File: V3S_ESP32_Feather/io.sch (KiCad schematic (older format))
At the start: 21 parts, among them J3 CAM, J7 Micro_SD_Card_Det, J9 I2C, U1 V3S, Y1 X1E0000210832, Y2 CC5V-T1A 32.768KHZ +-20PPM 12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

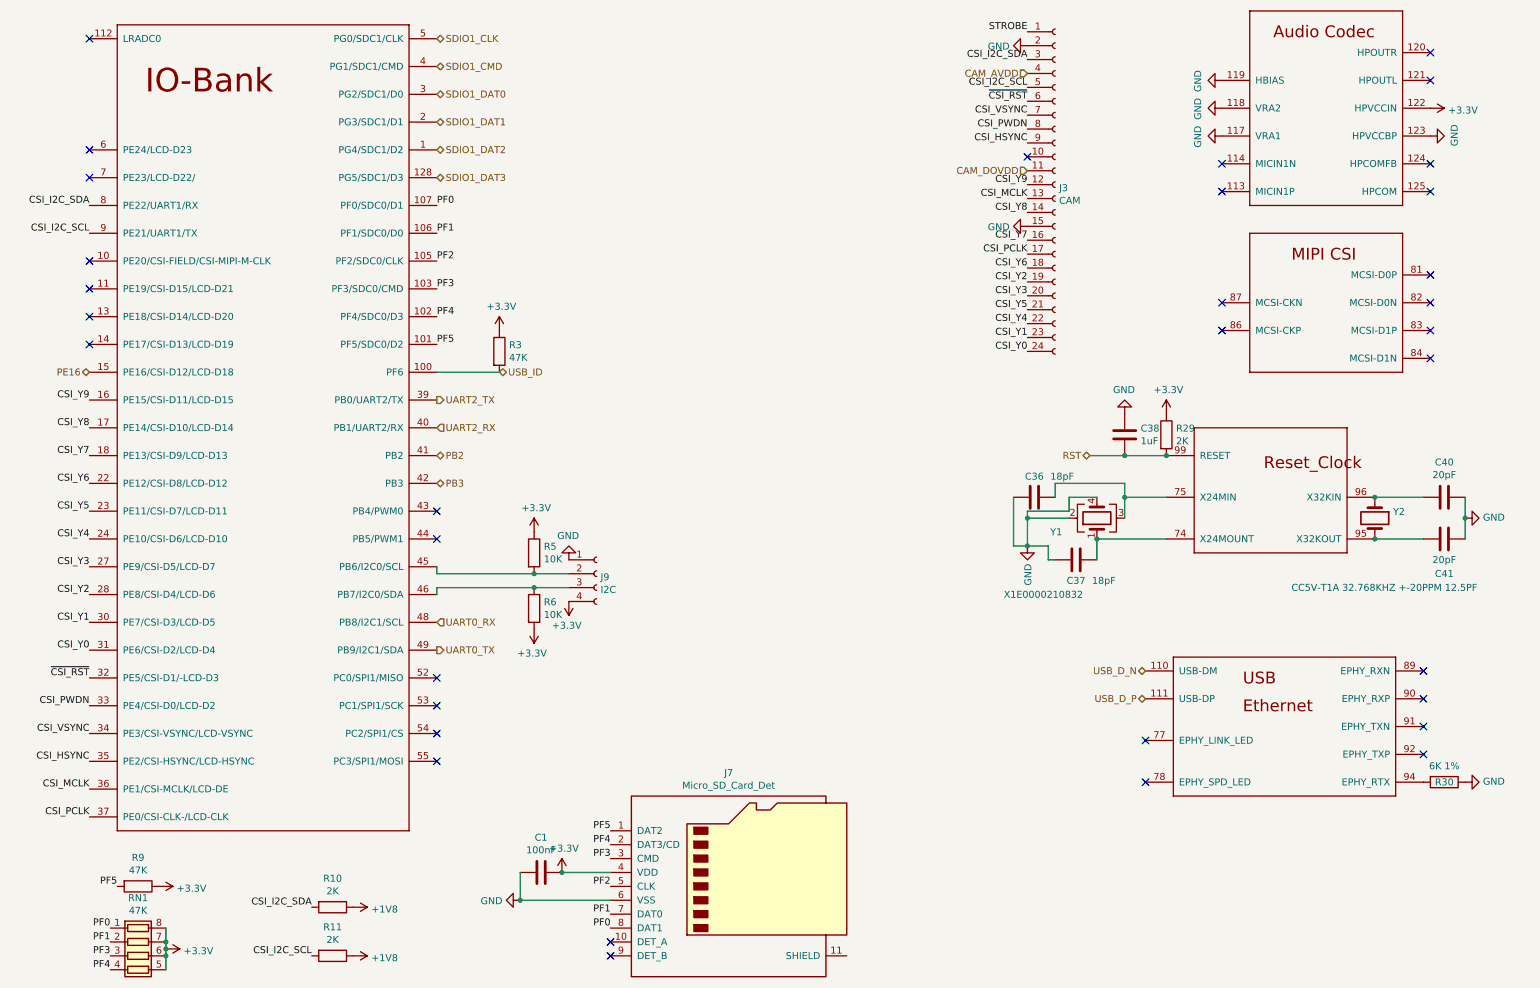
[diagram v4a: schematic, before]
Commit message: routing done, started filling bom
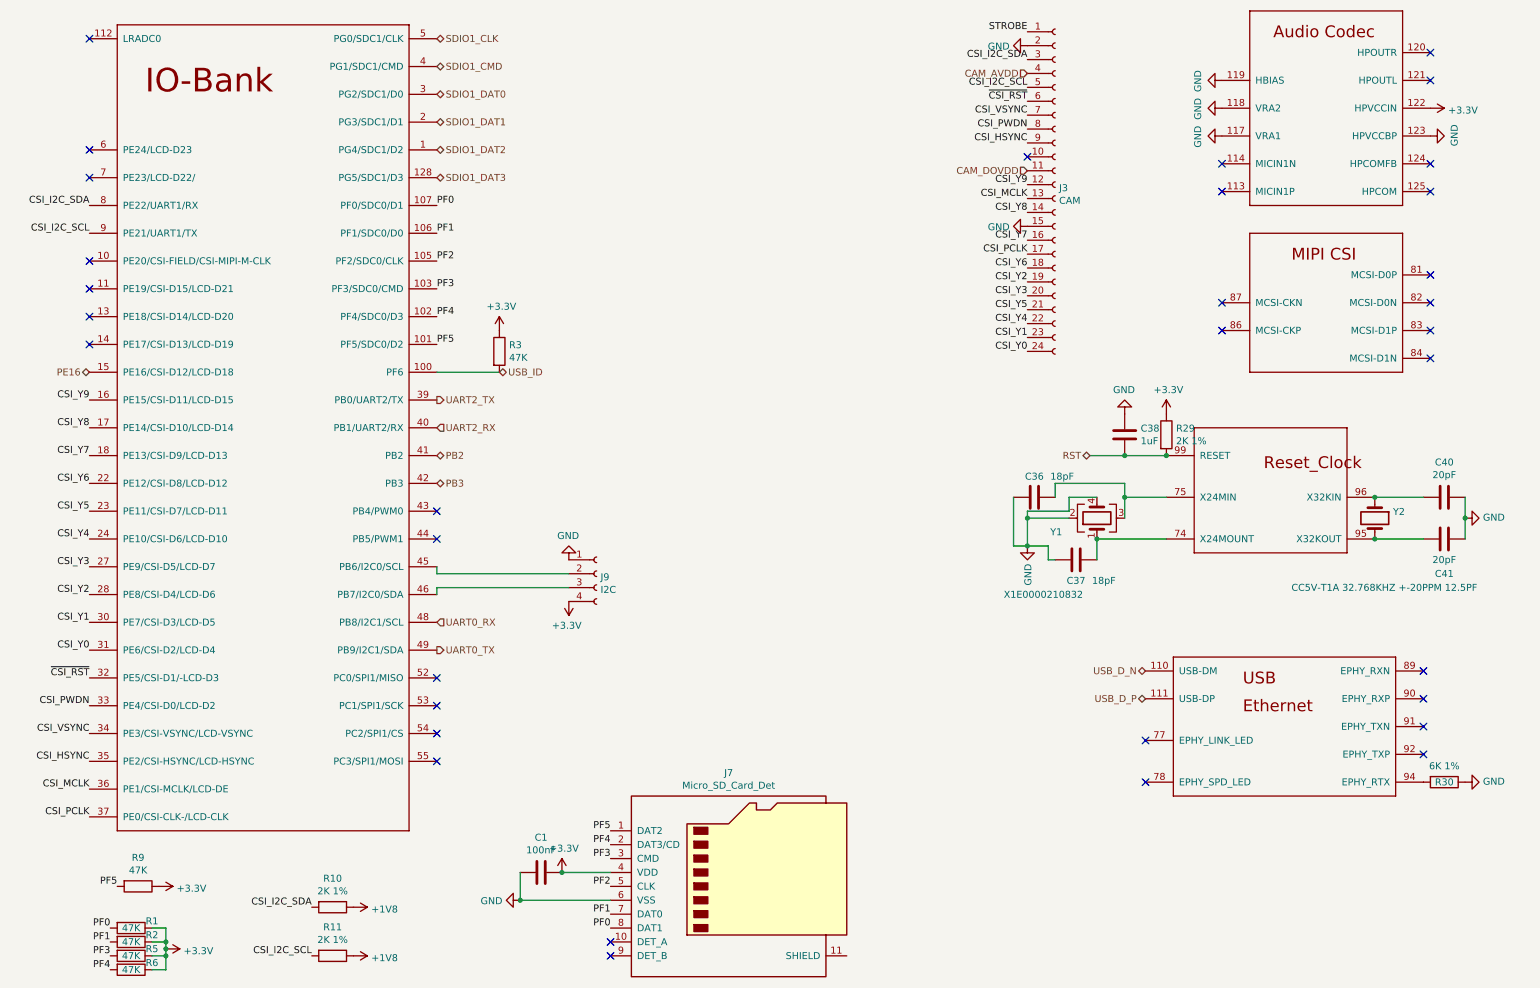
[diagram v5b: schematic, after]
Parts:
- removed RN1: 47K, Resistor_SMD:R_Array_Concave_4x0402, symbol Device:R_Pack04
- added R1, R2: 47K, Resistor_SMD:R_0201_0603Metric, symbol Device:R
- R10, R11, R29: value 2K -> 2K 1%
- R5, R6: value 10K -> 47K
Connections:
- net +3V3: now also R6.1, R1.1, R2.1; no longer R6.2
- net PF0: now also R1.2
- net PF1: now also R2.2
- net PF3: now also R5.2
- net PF4: now also R6.2
- net at J9.2 (Pin_2), U1.45 (PB6/I2C0/SCL): no longer R5.2
- net at J9.3 (Pin_3), U1.46 (PB7/I2C0/SDA): no longer R6.1
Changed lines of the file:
@@
 P 8750 3600
 F 0 "R29" H 8820 3646 50  0000 L CNN
-F 1 "2K" H 8820 3555 50  0000 L CNN
+F 1 "2K 1%" H 8820 3555 50  0000 L CNN
 F 2 "Resistor_SMD:R_0201_0603Metric" V 8680 3600 50  0001 C CNN
 F 3 "~" H 8750 3600 50  0001 C CNN
@@
 P 2750 7000
 F 0 "R10" V 2543 7000 50  0000 C CNN
-F 1 "2K" V 2634 7000 50  0000 C CNN
+F 1 "2K 1%" V 2634 7000 50  0000 C CNN
 F 2 "Resistor_SMD:R_0201_0603Metric" V 2680 7000 50  0001 C CNN
 F 3 "~" H 2750 7000 50  0001 C CNN
@@
 P 2750 7350
 F 0 "R11" V 2543 7350 50  0000 C CNN
-F 1 "2K" V 2634 7350 50  0000 C CNN
+F 1 "2K 1%" V 2634 7350 50  0000 C CNN
 F 2 "Resistor_SMD:R_0201_0603Metric" V 2680 7350 50  0001 C CNN
 F 3 "~" H 2750 7350 50  0001 C CNN
@@
 PF1
 $Comp
-L Device:R R9
-U 1 1 5D32DA86
-P 1350 6850
-F 0 "R9" V 1143 6850 50  0000 C CNN
-F 1 "47K" V 1234 6850 50  0000 C CNN
-F 2 "Resistor_SMD:R_0201_0603Metric" V 1280 6850 50  0001 C CNN
-F 3 "~" H 1350 6850 50  0001 C CNN
-	1    1350 6850
-	0    1    1    0
-$EndComp
-$Comp
-L Device:R_Pack04 RN1
-U 1 1 5D331F3F
-P 1350 7350
-F 0 "RN1" V 933 7350 50  0000 C CNN
-F 1 "47K" V 1024 7350 50  0000 C CNN
-F 2 "Resistor_SMD:R_Array_Concave_4x0402" V 1625 7350 50  0001 C CNN
-F 3 "~" H 1350 7350 50  0001 C CNN
-	1    1350 7350
-	0    1    1    0
-$EndComp
-$Comp
 L power:+3.3V #PWR0152
 U 1 1 5D336240
@@
 	0    1    1    0
 $EndComp
-Wire Wire Line
-	1550 7150 1550 7250
-Connection ~ 1550 7250
-Wire Wire Line
-	1550 7250 1550 7300
 Connection ~ 1550 7300
-Wire Wire Line
-	1550 7300 1550 7350
-Connection ~ 1550 7350
-Wire Wire Line
-	1550 7350 1550 7450
 NoConn ~ 1000 1550
 NoConn ~ 1000 1750
@@
 	3500 4550 3500 4600
 Wire Wire Line
-	4450 4700 4200 4700
-Wire Wire Line
 	3500 4700 3500 4750
-$Comp
-L Device:R R5
-U 1 1 5D898760
-P 4200 4450
-F 0 "R5" H 4270 4496 50  0000 L CNN
-F 1 "10K" H 4270 4405 50  0000 L CNN
-F 2 "Resistor_SMD:R_0201_0603Metric" V 4130 4450 50  0001 C CNN
-F 3 "~" H 4200 4450 50  0001 C CNN
-	1    4200 4450
-	1    0    0    -1
-$EndComp
-Connection ~ 4200 4600
-Wire Wire Line
-	4200 4600 4450 4600
-$Comp
-L Device:R R6
-U 1 1 5D89986A
-P 4200 4850
-F 0 "R6" H 4270 4896 50  0000 L CNN
-F 1 "10K" H 4270 4805 50  0000 L CNN
-F 2 "Resistor_SMD:R_0201_0603Metric" V 4130 4850 50  0001 C CNN
-F 3 "~" H 4200 4850 50  0001 C CNN
-	1    4200 4850
-	1    0    0    -1
-$EndComp
-Connection ~ 4200 4700
-Wire Wire Line
-	3500 4600 4200 4600
-Wire Wire Line
-	3500 4700 4200 4700
-$Comp
-L power:+3.3V #PWR0165
-U 1 1 5D89EBFE
-P 4200 4300
-F 0 "#PWR0165" H 4200 4150 50  0001 C CNN
-F 1 "+3.3V" H 4215 4473 50  0000 C CNN
-F 2 "" H 4200 4300 50  0001 C CNN
-F 3 "" H 4200 4300 50  0001 C CNN
-	1    4200 4300
-	1    0    0    -1
-$EndComp
-$Comp
-L power:+3.3V #PWR0171
-U 1 1 5D8A0291
-P 4200 5000
-F 0 "#PWR0171" H 4200 4850 50  0001 C CNN
-F 1 "+3.3V" H 4215 5173 50  0000 C CNN
-F 2 "" H 4200 5000 50  0001 C CNN
-F 3 "" H 4200 5000 50  0001 C CNN
-	1    4200 5000
-	-1   0    0    1
-$EndComp
 $Comp
 L power:GND #PWR0172
@@
 NoConn ~ 3500 5750
 NoConn ~ 3500 5950
+Wire Wire Line
+	3500 4600 4450 4600
+Wire Wire Line
+	3500 4700 4450 4700
+Wire Wire Line
+	1550 7300 1550 7350
+Wire Wire Line
+	1550 7150 1550 7250
+$Comp
+L Device:R R1
+U 1 1 5DC40187
+P 1300 7150
+F 0 "R1" V 1250 7300 50  0000 C CNN
+F 1 "47K" V 1300 7150 50  0000 C CNN
+F 2 "Resistor_SMD:R_0201_0603Metric" V 1230 7150 50  0001 C CNN
+F 3 "~" H 1300 7150 50  0001 C CNN
+	1    1300 7150
+	0    1    1    0
+$EndComp
+$Comp
+L Device:R R2
+U 1 1 5DC41033
+P 1300 7250
+F 0 "R2" V 1250 7400 50  0000 C CNN
+F 1 "47K" V 1300 7250 50  0000 C CNN
+F 2 "Resistor_SMD:R_0201_0603Metric" V 1230 7250 50  0001 C CNN
+F 3 "~" H 1300 7250 50  0001 C CNN
+	1    1300 7250
+	0    1    1    0
+$EndComp
+$Comp
+L Device:R R5
+U 1 1 5DC417A7
+P 1300 7350
+F 0 "R5" V 1250 7500 50  0000 C CNN
+F 1 "47K" V 1300 7350 50  0000 C CNN
+F 2 "Resistor_SMD:R_0201_0603Metric" V 1230 7350 50  0001 C CNN
+F 3 "~" H 1300 7350 50  0001 C CNN
+	1    1300 7350
+	0    1    1    0
+$EndComp
+$Comp
+L Device:R R6
+U 1 1 5DC41DCE
+P 1300 7450
+F 0 "R6" V 1250 7600 50  0000 C CNN
+F 1 "47K" V 1300 7450 50  0000 C CNN
+F 2 "Resistor_SMD:R_0201_0603Metric" V 1230 7450 50  0001 C CNN
+F 3 "~" H 1300 7450 50  0001 C CNN
+	1    1300 7450
+	0    1    1    0
+$EndComp
+Wire Wire Line
+	1450 7150 1550 7150
+Wire Wire Line
+	1450 7250 1550 7250
+Connection ~ 1550 7250
+Wire Wire Line
+	1550 7250 1550 7300
+Wire Wire Line
+	1450 7350 1550 7350
+Connection ~ 1550 7350
+Wire Wire Line
+	1550 7350 1550 7450
+Wire Wire Line
+	1450 7450 1550 7450
+$Comp
+L Device:R R9
+U 1 1 5D32DA86
+P 1350 6850
+F 0 "R9" V 1143 6850 50  0000 C CNN
+F 1 "47K" V 1234 6850 50  0000 C CNN
+F 2 "Resistor_SMD:R_0201_0603Metric" V 1280 6850 50  0001 C CNN
+F 3 "~" H 1350 6850 50  0001 C CNN
+	1    1350 6850
+	0    1    1    0
+$EndComp
 $EndSCHEMATC

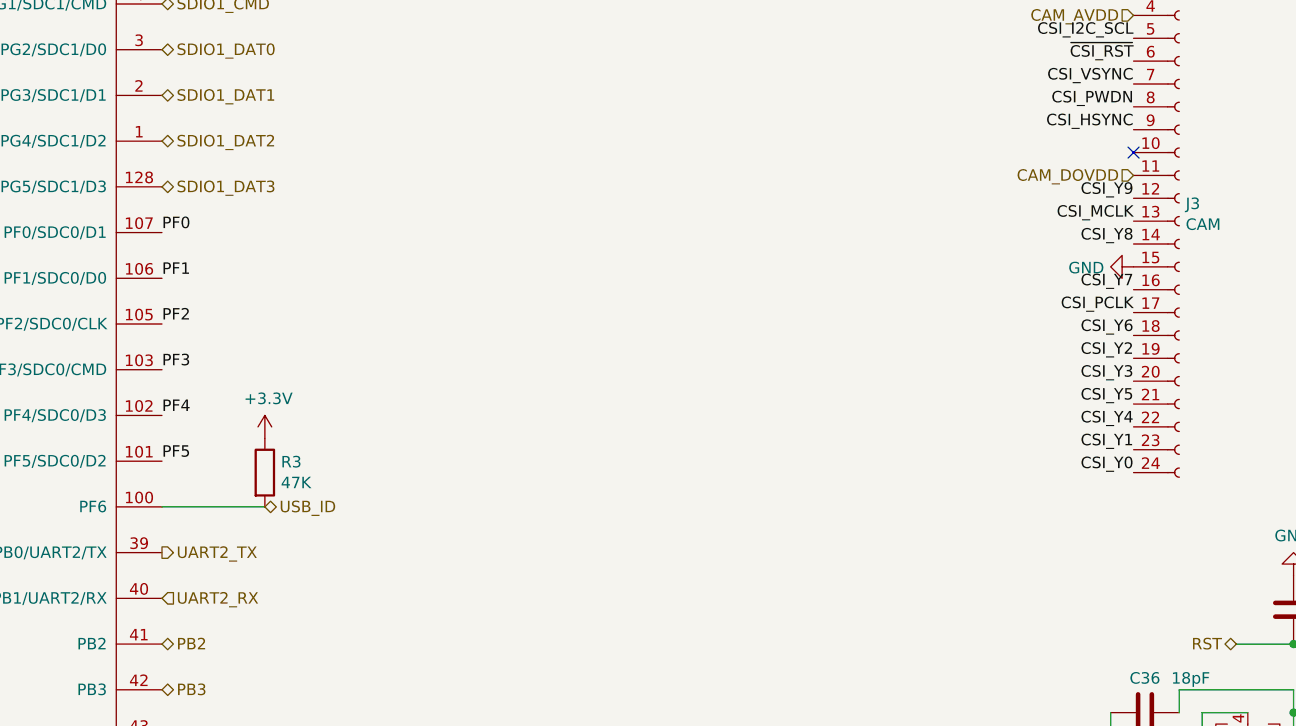
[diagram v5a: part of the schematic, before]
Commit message: Apply V3s design guide recommendations
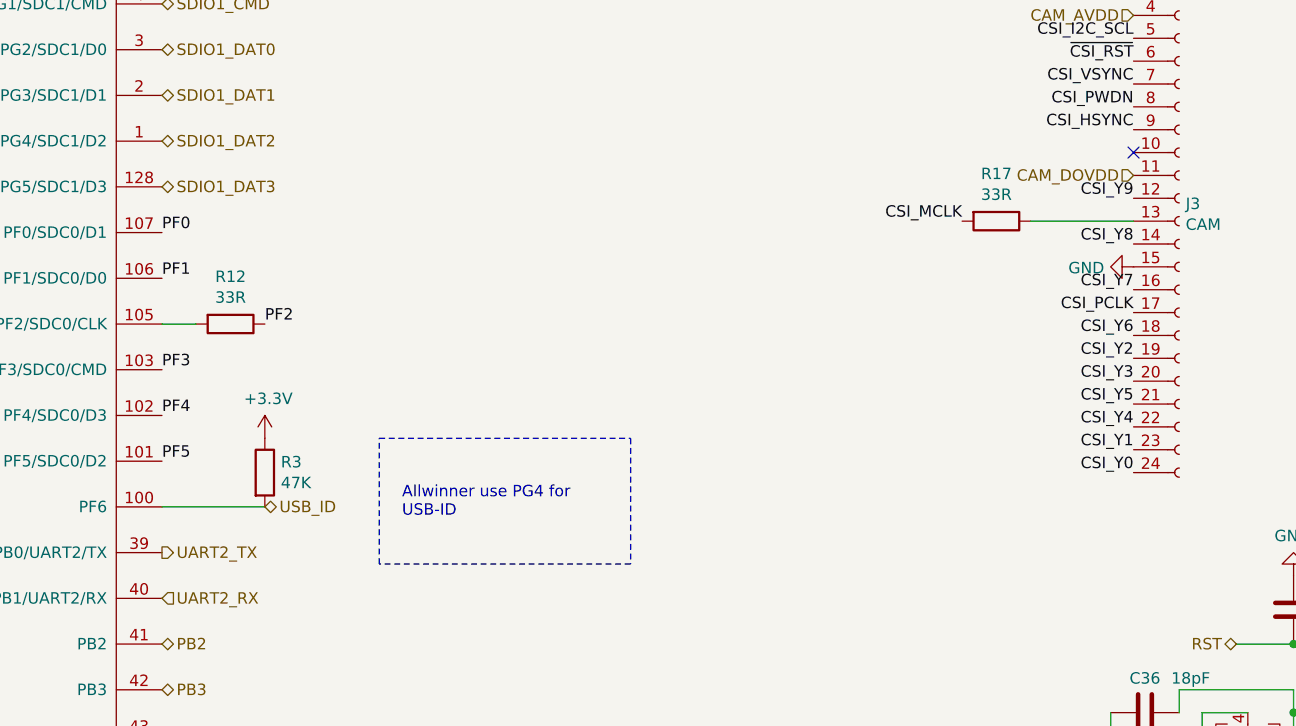
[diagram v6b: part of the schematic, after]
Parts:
- added R12, R17: 33R, Resistor_SMD:R_0201_0603Metric, symbol Device:R
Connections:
- net CSI_MCLK: now also R17.2; no longer J3.13 (Pin_13)
- net PF2: now also R12.1; no longer U1.105 (PF2/SDC0/CLK)
- new net: R12.2, U1.105 (PF2/SDC0/CLK)
- new net: J3.13 (Pin_13), R17.1
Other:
- note added: "Allwinner use PG4 for \nUSB-ID"
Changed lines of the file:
@@
 Text Label 1000 5550 2    50   ~ 0
 CSI_PWDN
-$Comp
-L OB-rescue:V3S-v3s U1
-U 2 1 5BA7737C
-P 2200 3550
-F 0 "U1" H 2250 3600 50  0001 C CNN
-F 1 "V3S" H 2200 3550 50  0001 C CNN
-F 2 "V3s:LQFP-128_14x14mm_P0.4mm" H 2200 3550 50  0001 C CNN
-F 3 "" H 2200 3550 50  0001 C CNN
-	2    2200 3550
-	1    0    0    -1
-$EndComp
 Text Label 1000 2150 2    50   ~ 0
 CSI_I2C_SCL
@@
 Text Label 3500 2150 0    50   ~ 0
 PF1
-Text Label 3500 2350 0    50   ~ 0
+Text Label 3950 2350 0    50   ~ 0
 PF2
 Text Label 3500 2550 0    50   ~ 0
@@
 Text Label 7750 2300 2    50   ~ 0
 CSI_PCLK
-Text Label 7750 1900 2    50   ~ 0
+Text Label 7000 1900 2    50   ~ 0
 CSI_MCLK
 Text Label 7750 900  2    50   ~ 0
@@
 	0    1    1    0
 $EndComp
+$Comp
+L OB-rescue:V3S-v3s U1
+U 2 1 5BA7737C
+P 2200 3550
+F 0 "U1" H 2250 3600 50  0001 C CNN
+F 1 "V3S" H 2200 3550 50  0001 C CNN
+F 2 "V3s:LQFP-128_14x14mm_P0.4mm" H 2200 3550 50  0001 C CNN
+F 3 "" H 2200 3550 50  0001 C CNN
+	2    2200 3550
+	1    0    0    -1
+$EndComp
+$Comp
+L Device:R R17
+U 1 1 5DC3C075
+P 7150 1900
+F 0 "R17" V 6943 1900 50  0000 C CNN
+F 1 "33R" V 7034 1900 50  0000 C CNN
+F 2 "Resistor_SMD:R_0201_0603Metric" V 7080 1900 50  0001 C CNN
+F 3 "~" H 7150 1900 50  0001 C CNN
+	1    7150 1900
+	0    1    1    0
+$EndComp
+Wire Wire Line
+	7750 1900 7300 1900
+$Comp
+L Device:R R12
+U 1 1 5DC3FE0F
+P 3800 2350
+F 0 "R12" V 3593 2350 50  0000 C CNN
+F 1 "33R" V 3684 2350 50  0000 C CNN
+F 2 "Resistor_SMD:R_0201_0603Metric" V 3730 2350 50  0001 C CNN
+F 3 "~" H 3800 2350 50  0001 C CNN
+	1    3800 2350
+	0    1    1    0
+$EndComp
+Wire Wire Line
+	3650 2350 3500 2350
+Wire Notes Line
+	4450 2850 5550 2850
+Wire Notes Line
+	5550 2850 5550 3400
+Wire Notes Line
+	5550 3400 4450 3400
+Wire Notes Line
+	4450 3400 4450 2850
+Text Notes 4550 3200 0    50   ~ 0
+Allwinner use PG4 for \nUSB-ID
 $EndSCHEMATC

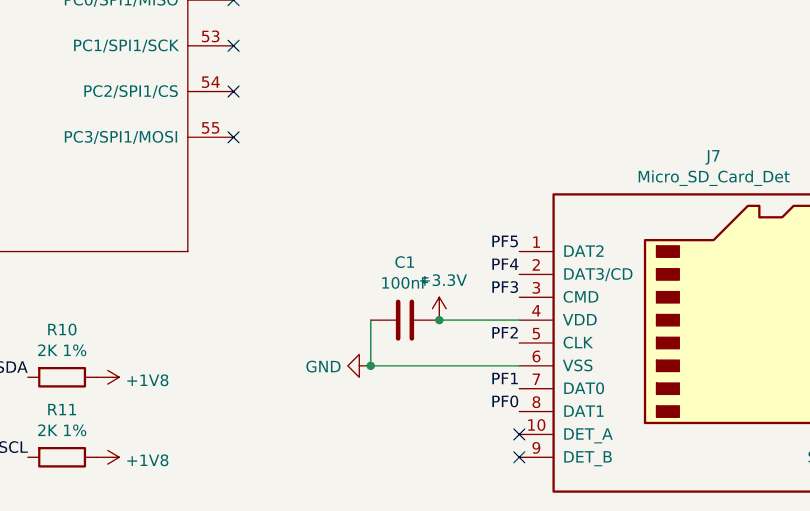
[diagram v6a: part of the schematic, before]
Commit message: Move via from pad and rebuild fab files
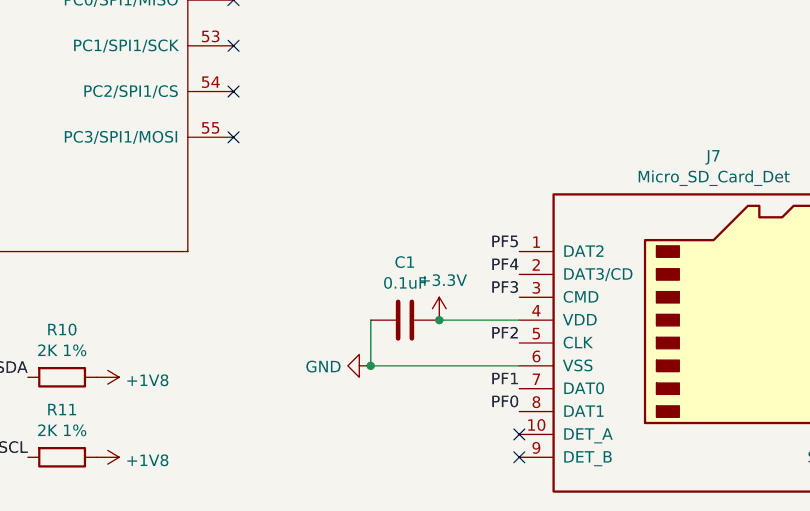
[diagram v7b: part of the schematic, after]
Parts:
- C1: value 100nF -> 0.1uF
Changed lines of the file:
@@
 P 4250 6750
 F 0 "C1" V 3998 6750 50  0000 C CNN
-F 1 "100nF" V 4089 6750 50  0000 C CNN
+F 1 "0.1uF" V 4089 6750 50  0000 C CNN
 F 2 "Capacitor_SMD:C_0201_0603Metric" H 4288 6600 50  0001 C CNN
 F 3 "~" H 4250 6750 50  0001 C CNN
